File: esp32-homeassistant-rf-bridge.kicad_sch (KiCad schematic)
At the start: 35 parts, among them J1 USB_C_Receptacle_USB2.0_16P, J2 Conn_02x04_Odd_Even, SW1 SW_Push, SW2 SW_Push, SW3 SW_Push, SW4 SW_Push, U1 ESP32-S2-MINI-1, U2 TSOP41xx, U3 XC6206P332MR, U4 CC1101_E07-M1101D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

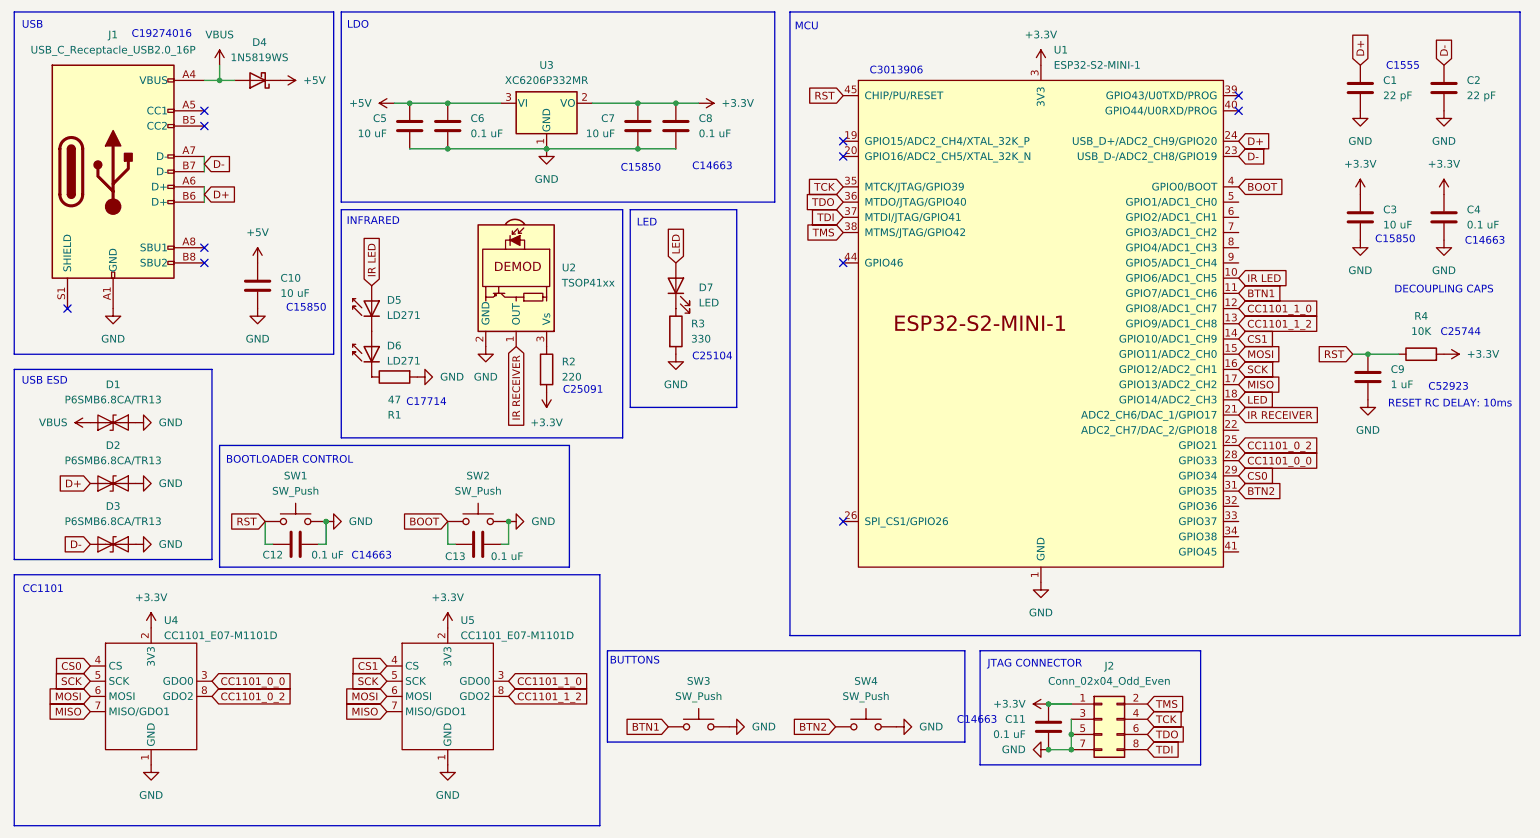
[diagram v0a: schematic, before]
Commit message: update some silkscreen stuff
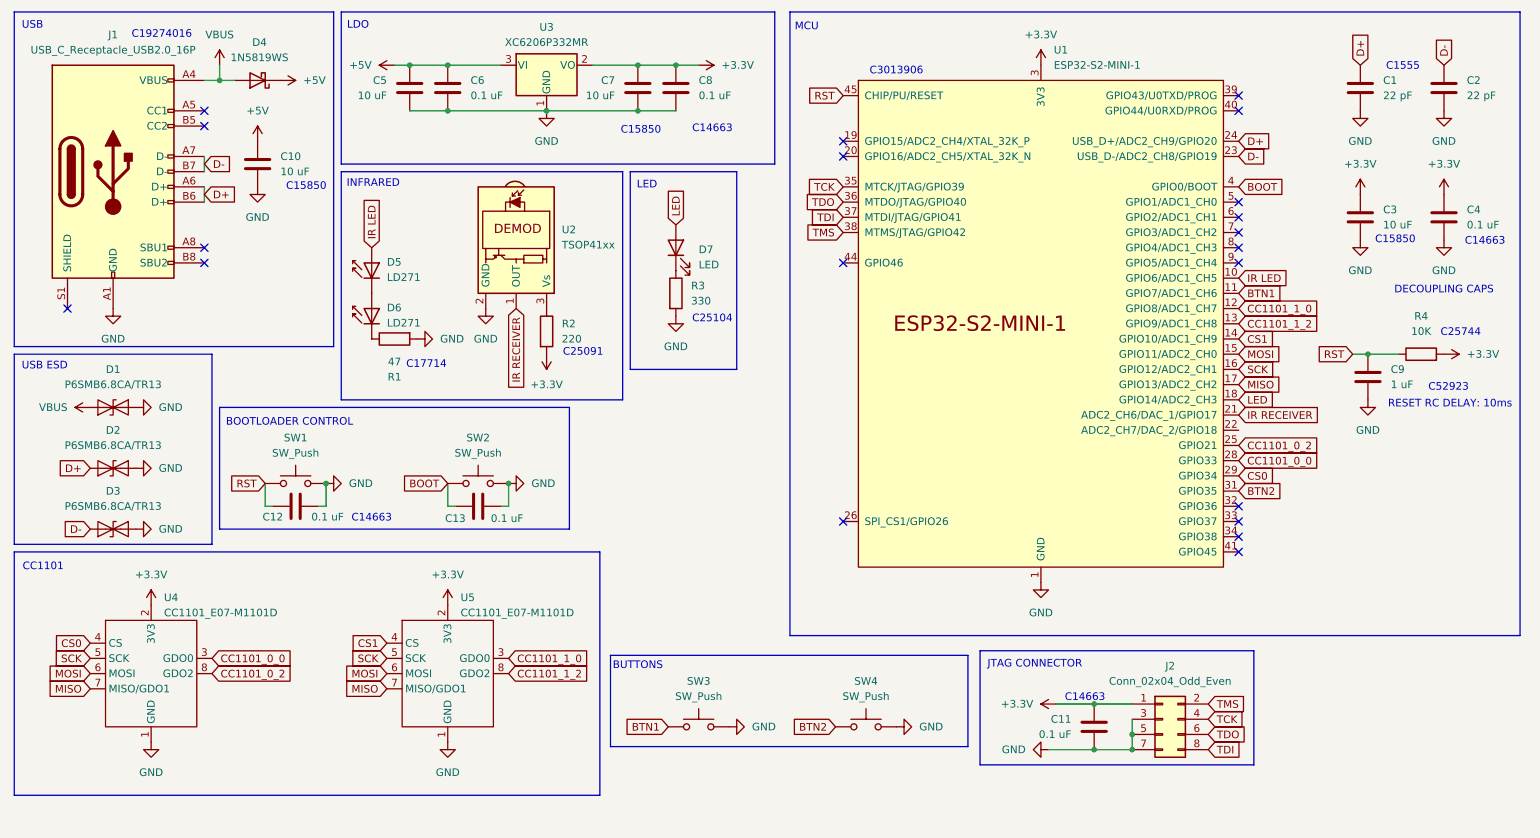
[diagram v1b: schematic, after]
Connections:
- no-connect marks 11 -> 20
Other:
- moved on the sheet: C10, C11, C12, C13, C5, C6, C7, C8, D1, D2, D3, D5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
